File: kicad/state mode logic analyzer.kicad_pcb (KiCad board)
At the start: 4 copper layers, 80.7 x 56.7 mm, 128 parts, among them J1 USB0, J2 Exp Out, J3 CLK 0-7, J4 8-15, J5 Exp In, J7 SWD0, J9 5V USB0, SW1 Reset 0, SW2 Boot 0, U1 RP2040, U10 74LVC245APW, U11 74LVC245APW, U3 74HC4520D, U4 LTC6994xS6-1, U5 MCP4725, U6 AD5241BRZ1M, U7 IS25LP128F-JBLE, U9 MCP1826S, Y1 ECS-120-18-33-JEM-TR

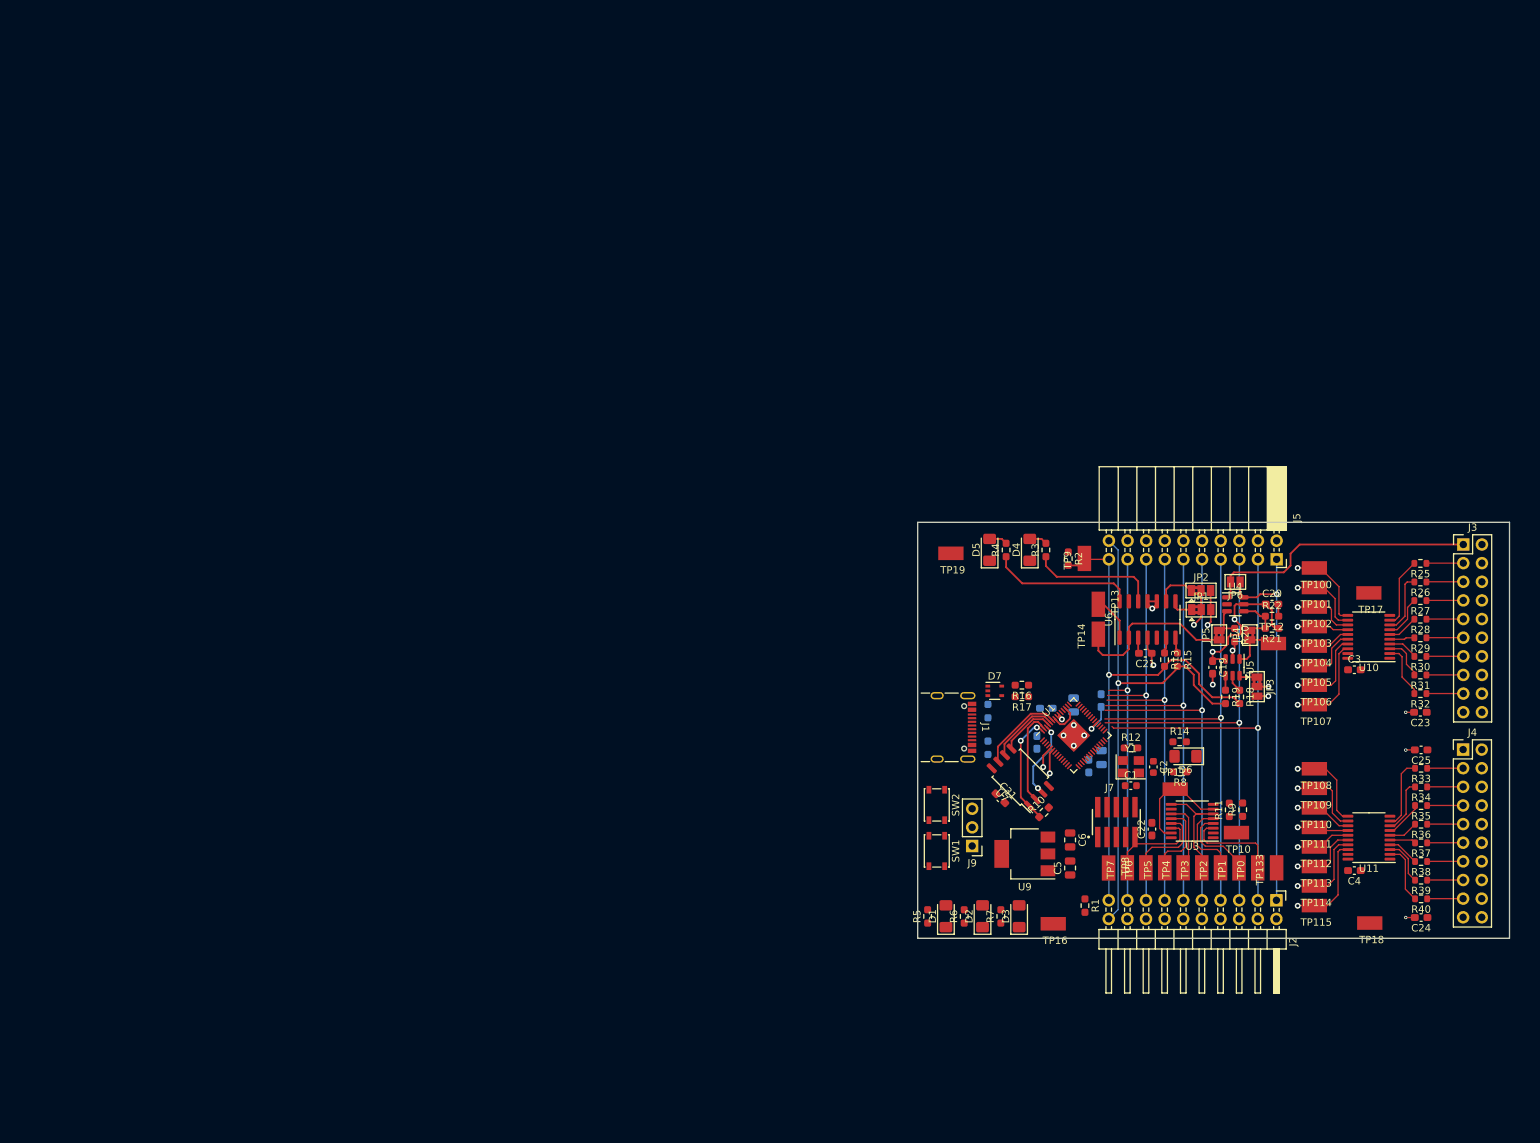
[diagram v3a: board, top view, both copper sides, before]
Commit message: passed drc and started silk clean up
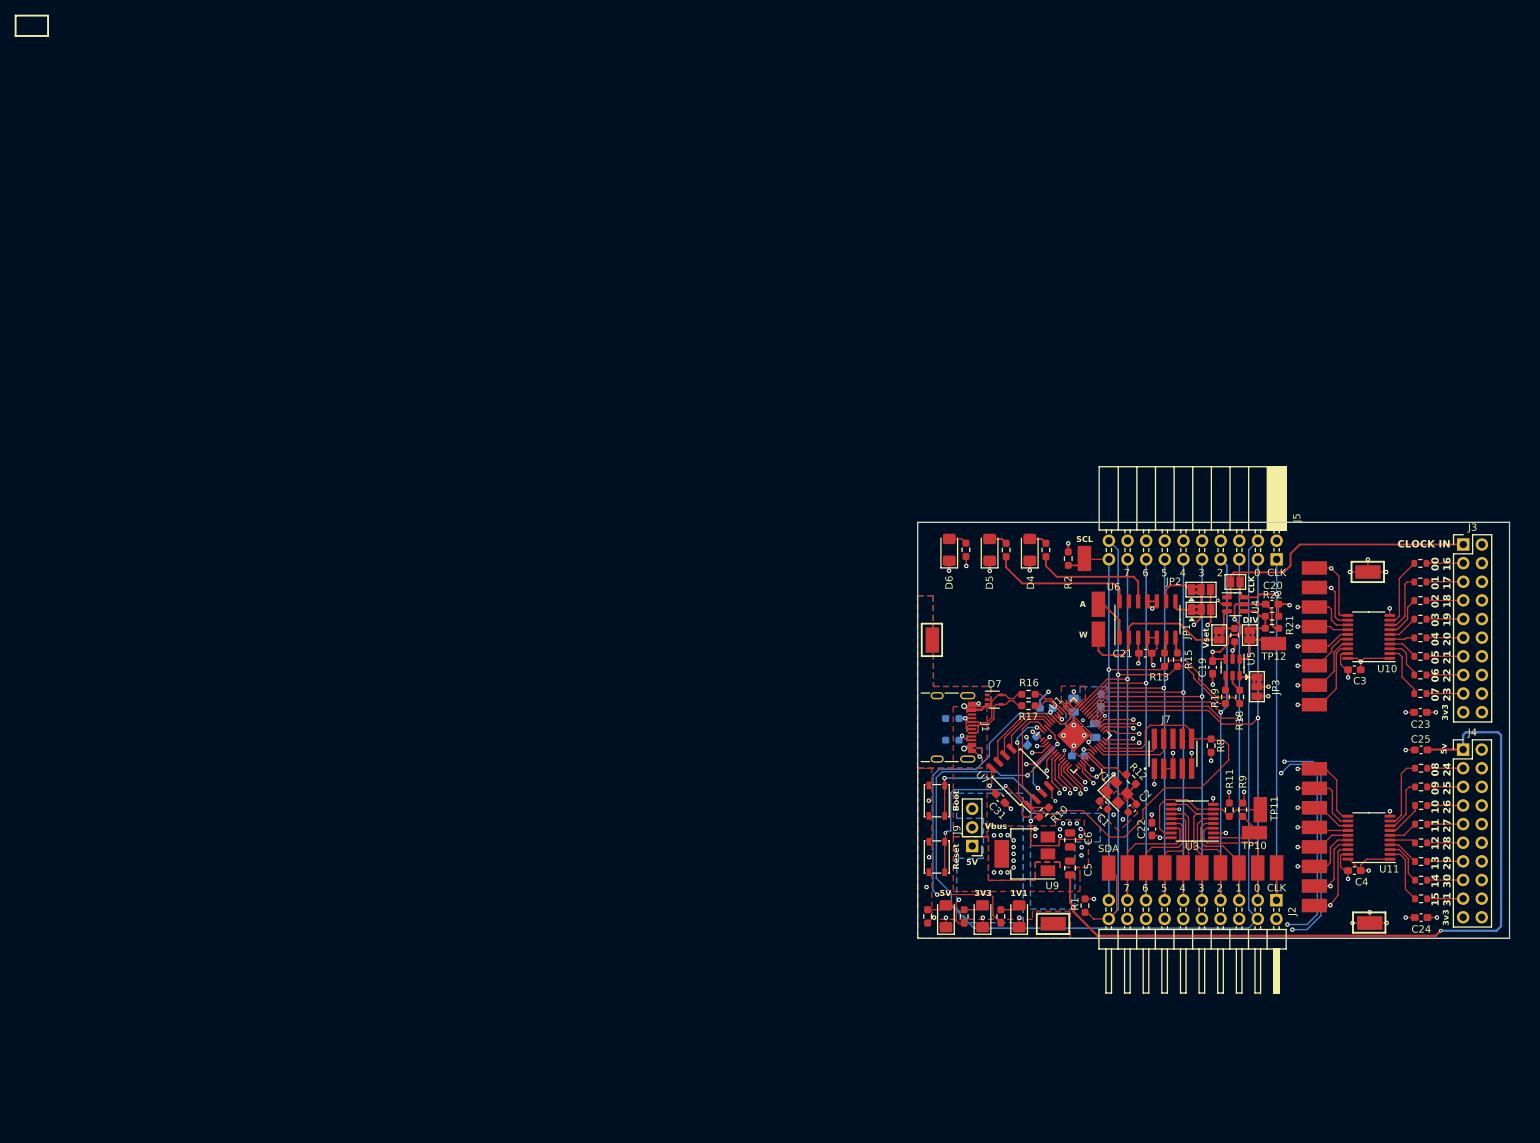
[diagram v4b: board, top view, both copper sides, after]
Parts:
- moved D6 42.8 mm to (122.8, 70.0), turned to 90 degrees
- moved R14 39.2 mm to (125.1, 70.0), turned to 90 degrees
- moved J7 12.1 mm to (153.3, 97.8)
- moved TP19 12.1 mm to (120.5, 82.3), turned to 90 degrees
- moved TP11 11.9 mm to (165.2, 105.5), turned to -90 degrees
- moved C2 6.32 mm to (147.8, 105.3), turned to -135 degrees
- moved R8 5.53 mm to (158.6, 96.8), turned to 90 degrees
- moved R24 4.96 mm to (123.3, 96.0), turned to 180 degrees
- moved R23 4.96 mm to (123.3, 93.0), turned to 180 degrees
- moved C1 4.57 mm to (143.9, 104.8), turned to -45 degrees
- moved R12 4.28 mm to (147.6, 101.3), turned to -45 degrees
- moved Y1 3.95 mm to (145.7, 103.1), turned to -45 degrees
- moved C12 3.80 mm to (142.8, 94.7), turned to 90 degrees
- moved TP17 2.85 mm to (179.9, 73.1)
- moved TP10 2.45 mm to (164.4, 108.6)
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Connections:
- U1 pad 11: /BUF10 -> /BUF13
- U1 pad 12: /BUF09 -> /BUF12
- U1 pad 13: /BUF08 -> /BUF11
- U1 pad 14: /BUF07 -> /BUF10
- U1 pad 15: /BUF06 -> /BUF09
- U1 pad 16: /BUF05 -> /BUF08
- U1 pad 17: /BUF04 -> /BUF07
- U1 pad 18: /BUF03 -> /BUF06
- U1 pad 27: /BUF02 -> /BUF05
- U1 pad 28: /BUF01 -> /BUF04
- U1 pad 29: /BUF00 -> /BUF03
- U1 pad 30: /TS0 -> /BUF02
- U1 pad 31: /TS1 -> /BUF01
- U1 pad 32: /TS2 -> /BUF00
- U1 pad 34: /TS3 -> /TS0
- U1 pad 35: /TS4 -> /TS1
- U1 pad 36: /TS5 -> /TS2
- U1 pad 37: /TS6 -> /TS3
- U1 pad 38: /TS7 -> /TS4
- U1 pad 39: /CNT_CLK -> /TS5
- U1 pad 4: /CLK -> /CNT_CLK
- U1 pad 40: /CNT_RESET -> /TS6
- U1 pad 41: /LA_Enable -> /TS7
- U1 pad 5: /BUF15 -> /CNT_RESET
- U1 pad 6: /BUF14 -> /LA_Enable
- U1 pad 7: /BUF13 -> /CLK
- U1 pad 8: /BUF12 -> /BUF15
- U1 pad 9: /BUF11 -> /BUF14
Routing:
- net /CNT_RESET: track 0.00 -> 133.8 mm, vias 0 -> 5
- net /LA_Enable: track 0.00 -> 132.3 mm, vias 0 -> 1
- net +5V: track 0.00 -> 117.0 mm, vias 0 -> 2
- net /CNT_CLK: track 0.00 -> 97.4 mm, vias 0 -> 4
- net /Run: track 0.00 -> 82.6 mm, vias 0 -> 2
- net +3V3: track 37.3 -> 116.4 mm, vias 7 -> 33
- net /CLK: track 53.5 -> 115.9 mm, vias 1 -> 2
- net GND: track 21.9 -> 80.2 mm, vias 12 -> 61
- net +1V1: track 4.41 -> 61.8 mm, vias 0 -> 3
- net /BUF15: track 16.6 -> 61.5 mm
- net /BUF14: track 14.9 -> 59.1 mm
- net /BUF09: track 10.4 -> 53.4 mm, vias 1 -> 2
- net /BUF13: track 9.59 -> 50.9 mm, vias 1 -> 2
- net /BUF11: track 7.06 -> 47.9 mm, vias 1 -> 2
- net /BUF10: track 7.85 -> 48.6 mm, vias 1 -> 2
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- added copper zone on B.Cu, net +3V3
- added copper zone on F.Cu, net +3V3
- added copper zone on In2.Cu, net +3V3
- added copper zone on F.Cu, net +5V
- added copper zone on F.Cu, net /VBUS
- added copper zone on B.Cu, net GND
- added copper zone on F.Cu, net GND
- added copper zone on In1.Cu, net GND
- added copper zone on In2.Cu, net GND
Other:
- board text added: "0"
- board text added: "00 16"
- board text added: "01 17"
- board text added: "02 18"
- board text added: "03 19"
- board text added: "04 20"
- board text added: "05 21"
- board text added: "06 22"
- board text added: "07 23"
- board text added: "08 24"
- board text added: "09 25"
- board text added: "1"
- board text added: "10 26"
- board text added: "11 27"
- board text added: "12 28"
- board text added: "13 29"
- board text added: "14 30"
- board text added: "15 31"
- board text added: "1V1"
- board text added: "2"
- board text added: "3"
- board text added: "3V3"
- board text added: "3v3"
- board text added: "4"
- board text added: "5"
- board text added: "5V"
- board text added: "5v"
- board text added: "6"
- board text added: "7"
- board text added: "A"
- board text added: "Boot"
- board text added: "CLK"
- board text added: "CLOCK IN"
- board text added: "DIV"
- board text added: "Reset"
- board text added: "SCL"
- board text added: "SDA"
- board text added: "Vbus"
- board text added: "Vset"
- board text added: "W"

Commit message: rev1 before verification
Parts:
- added REF**: KiCad-Logo_5mm_SilkScreen, Symbol:KiCad-Logo_5mm_SilkScreen, B.Cu at (132.4, 80.2)
- added REF**: OSHW-Symbol_8.9x8mm_SilkScreen, Symbol:OSHW-Symbol_8.9x8mm_SilkScreen, B.Cu at (179.2, 95.1)
- added TP15: TestPoint_Harwin, My Libraries:Harwin-S1751-46-Test-Point, F.Cu at (120.6, 78.2)
- added svg2mod: G***, My Libraries:BE5v2, F.Cu at (177.4, 92.4)
- moved TP19 2.43 mm to (120.5, 84.8)
- moved TP10 1.30 mm to (163.2, 108.7)
- moved TP18 0.73 mm to (180.2, 120.2)
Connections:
- net Net-(JP1-A) renamed /AD0
- net Net-(JP2-A) renamed /AD1
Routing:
- net +5V: track 117.0 -> 102.2 mm
- net GND: track 80.2 -> 81.3 mm, vias 61 -> 63
- net +3V3: vias 33 -> 37
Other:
- board size 80.7 x 56.7 mm -> 79 x 56.7 mm
- board text added: "A0"
- board text added: "AD0"
- board text added: "AD1"
- board text added: "ARM"
- board text added: "CNT_CLK"
- board text added: "DAC"
- board text added: "RST"
- board text added: "State Mode LA rev 1 - 2023-10-21"
- board text added: "TRIG"
- board text removed: "3v3"
- board text removed: "5v"
- board text removed: "need to setup Z for diff pair"

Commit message: rneed to review again
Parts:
- removed the C24 at (187.2, 120.2)
- removed J3: CLK 0-7, Connector_PinHeader_2.54mm:PinHeader_2x10_P2.54mm_Vertical
- removed J4: 8-15, Connector_PinHeader_2.54mm:PinHeader_2x10_P2.54mm_Vertical
- added H1: MountingHole, MountingHole:MountingHole_2.7mm, F.Cu at (194.0, 69.7)
- added H2: MountingHole, MountingHole:MountingHole_2.7mm, F.Cu at (126.5, 79.1)
- added H3: MountingHole, MountingHole:MountingHole_2.7mm, F.Cu at (179.5, 102.4)
- added J6: Probe, Connector_PinHeader_2.54mm:PinHeader_2x12_P2.54mm_Vertical, F.Cu at (195.6, 79.5)
- added J8: Probe Power, Connector_PinHeader_2.54mm:PinHeader_1x03_P2.54mm_Vertical, F.Cu at (198.0, 118.2)
- moved C23 22.0 mm to (193.8, 113.2)
- moved C24 21.9 mm to (193.8, 118.2)
- moved REF** 4.58 mm to (136.9, 79.4)
- moved TP18 1.91 mm to (181.0, 118.5)
- moved TP17 0.22 mm to (180.1, 73.2)
- renumbered C25 to C24
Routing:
- net +5V: track 102.2 -> 81.3 mm, vias 2 -> 1
- net /IN00: track 4.99 -> 16.3 mm
- net /IN14: track 4.88 -> 15.5 mm
- net /IN_CLK: track 37.6 -> 48.1 mm
- net /IN10: track 4.89 -> 14.2 mm
- net /IN12: track 4.89 -> 13.5 mm
- net /IN15: track 4.88 -> 13.3 mm
- net /IN02: track 5.00 -> 13.4 mm
- net /IN04: track 5.01 -> 13.4 mm
- net /IN06: track 5.02 -> 12.3 mm
- net /IN08: track 4.90 -> 12.2 mm
- net /IN13: track 4.89 -> 11.5 mm
- net /IN11: track 4.89 -> 11.4 mm
- net /IN01: track 4.99 -> 10.8 mm
- net /IN09: track 4.90 -> 9.99 mm
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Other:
- board size 79 x 56.7 mm -> 82.8 x 56.7 mm
- board text added: "00"
- board text added: "01|00"
- board text added: "03|02"
- board text added: "05|04"
- board text added: "07"
- board text added: "07|06"
- board text added: "08"
- board text added: "09|08"
- board text added: "11|10"
- board text added: "13|12"
- board text added: "15"
- board text added: "15|14"
- board text removed: "00 16"
- board text removed: "01 17"
- board text removed: "02 18"
- board text removed: "03 19"
- board text removed: "04 20"
- board text removed: "05 21"
- board text removed: "06 22"
- board text removed: "07 23"
- board text removed: "08 24"
- board text removed: "09 25"
- board text removed: "10 26"
- board text removed: "11 27"
- board text removed: "12 28"
- board text removed: "13 29"
- board text removed: "14 30"
- board text removed: "15 31"

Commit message: Deocrated schematic
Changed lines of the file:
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@@
   (gr_rect (start 166.125 119.0125) (end 168.75 121.7875)
     (stroke (width 0.254) (type default)) (fill none) (layer "B.SilkS"))
-  (gr_rect (start 192.596875 88.428126) (end 201.203126 85.875)
+  (gr_rect (start 192.596875 85.875) (end 201.203126 88.428126)
     (stroke (width 0.254) (type solid)) (fill solid) (layer "B.SilkS"))
-  (gr_rect (start 192.571875 96.078126) (end 201.178126 93.525)
+  (gr_rect (start 192.571875 93.525) (end 201.178126 96.078126)
     (stroke (width 0.254) (type solid)) (fill solid) (layer "B.SilkS"))
-  (gr_rect (start 192.596875 103.628126) (end 201.203126 101.075)
+  (gr_rect (start 192.596875 101.075) (end 201.203126 103.628126)
     (stroke (width 0.254) (type solid)) (fill solid) (layer "B.SilkS"))
   (gr_rect (start 166.2 67.4375) (end 168.825 70.2125)
@@
   (gr_rect (start 149.2 75.775) (end 151.775 78.55)
     (stroke (width 0.15) (type default)) (fill none) (layer "F.SilkS"))
-  (gr_rect (start 192.45 80.75) (end 196.75 78.45)
+  (gr_rect (start 192.45 78.45) (end 196.75 80.75)
     (stroke (width 0.15) (type solid)) (fill solid) (layer "F.SilkS"))
   (gr_rect (start 192.596874 85.875) (end 201.203125 88.428126)
@@
   (gr_circle (center 160.55 109.3) (end 160.45 109.4)
     (stroke (width 0.15) (type default)) (fill none) (layer "F.SilkS"))
-  (gr_rect (start 201.206251 114.323437) (end 195.625 116.876563)
+  (gr_rect (start 195.625 114.323437) (end 201.206251 116.876563)
     (stroke (width 0.254) (type solid)) (fill solid) (layer "F.SilkS"))
   (gr_poly
